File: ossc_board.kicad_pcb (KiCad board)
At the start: 2 copper layers, 91.2 x 167 mm, 343 parts, among them J1 HDMI_CONN (10029449-111RLF), J10 COLOR INPUT, J11 MONO INPUT, J12 NEXT PWR INPUT 1, J13 NEXT PWR INPUT 2, J14 -12VDC OUT, J15 5VDC STANDBY, J16 MON IN 1, J17 MON IN 2, J18 PA1, J19 BOOT0, J2 OUT (SJ1-3535NG), J20 PC0, J21 PC1, J22 PB0, J23 PB1, J24 R SPK, J25 R SPEAKER (SJ-2509N), J26 L SPEAKER, J27 L SPK, J28 I2C Ext, J29 OLED, J3 MIC (SJ1-3535NG), J30 BOOT1, J31 NeXT Keyboard, J32 NeXT Keyboard (MD-50SM / KMDG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, J4 USB Host (SS-52100-001), J5 Mic IN, J6 Audio OUT, J7 STLINK, J8 UART2, J9 PA0, P1 JTAG (30310-6002HB), Q1 2SC2712, SW1 NeXT POWER SW (1-1825027-1 / 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, SW2 BTN0, SW3 NeXT POWER SW, SW4 MCU RESET, U1 TVP7002PZP, U10 S25FL216K (IS25LP016D-JBLE), U11 TLV70033DDCR, U12 TLV70012DDCT, U13 TLV70025DDCT, U14 TLV70012DDCT, U15 TLV70018DDCT, U16 TLV70018DDCT, U17 USBLC6-2SC6, U18 STMPS2151STR‎ or TPS2051CDBV, U19 SN74LVC2G34DBV, U2 EP4CE15E22C8N, U20 PCM5122PW, U21 TLV70033DDCR (or XC6204B332MR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, U22 TLV70033DDCR (or XC6204B332MR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, U23 PLT133/T, U24 STM32F401RCT6, U25 SN74LVC1G07DBV, U26 SN74HCT125DR, U27 TLV320ADC3100, U28 BD33FC0FP, U29 TPA2005D1DGN, U3 IT6613E, U30 BD33FC0FP, U31 TPA2005D1DGN, U32 PCA9515AD, U4 SN74LVC2G17DBV, U5 BD33FC0FP, U6 TLV70033DDCR, U7 NCP703SN19T1G, U8 5V(DC/DC), U9 TLV70019DDCT, X1 ACHL-27MHZ-EK, X2 ASEDV-27.000MHZ-LR-T(ECS-2333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, X3 ECS-2520MVLC-225.792-BN-TR, Y2 25MHz (FA-238 25.0000MB-K0)

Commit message: update value
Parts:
- U26: value SN74HCT125DR -> SN74HC125DR
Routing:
- net GND: track 860.5 -> 860.1 mm, vias 373 -> 374
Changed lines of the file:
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@@
     (thickness 1.6)
     (drawings 182)
-    (tracks 4848)
+    (tracks 4852)
     (zones 0)
     (modules 343)
@@
       (effects (font (size 1 1) (thickness 0.15)) (justify mirror))
     )
-    (fp_text value SN74HCT125DR (at 0 -5.28 90) (layer B.Fab)
+    (fp_text value SN74HC125DR (at 0 -5.28 90) (layer B.Fab)
       (effects (font (size 1 1) (thickness 0.15)) (justify mirror))
     )
@@
   (via (at 104.6988 86.8934) (size 0.686) (drill 0.33) (layers F.Cu B.Cu) (net 87))
   (segment (start 91.7816 103.1748) (end 91.7816 101.6508) (width 0.4) (layer F.Cu) (net 87))
-  (segment (start 92.280672 101.151728) (end 91.7816 101.6508) (width 0.4) (layer F.Cu) (net 87))
-  (segment (start 92.280672 97.917872) (end 92.280672 101.151728) (width 0.4) (layer F.Cu) (net 87))
-  (segment (start 91.8152 97.4524) (end 92.280672 97.917872) (width 0.4) (layer F.Cu) (net 87))
-  (segment (start 90.7402 97.4524) (end 91.8152 97.4524) (width 0.4) (layer F.Cu) (net 87))
-  (segment (start 91.7816 103.1748) (end 93.599 103.1748) (width 0.4) (layer F.Cu) (net 87))
   (via (at 74.1 68.233) (size 0.686) (drill 0.35) (layers F.Cu B.Cu) (net 87))
   (via (at 120.7135 131.6482) (size 0.686) (drill 0.33) (layers F.Cu B.Cu) (net 87))
@@
   (via (at 105.1306 109.59592) (size 0.686) (drill 0.33) (layers F.Cu B.Cu) (net 87))
   (via (at 95.60052 104.96296) (size 0.686) (drill 0.33) (layers F.Cu B.Cu) (net 87))
-  (via (at 93.22816 102.13848) (size 0.686) (drill 0.33) (layers F.Cu B.Cu) (net 87))
+  (via (at 93.2688 102.6414) (size 0.686) (drill 0.33) (layers F.Cu B.Cu) (net 87))
   (via (at 94.71152 95.59544) (size 0.686) (drill 0.33) (layers F.Cu B.Cu) (net 87))
   (via (at 97.39884 96.5962) (size 0.686) (drill 0.33) (layers F.Cu B.Cu) (net 87))
@@
   (segment (start 63.1952 163.4363) (end 62.2935 162.5346) (width 0.25) (layer F.Cu) (net 87))
   (segment (start 63.7032 163.4363) (end 63.1952 163.4363) (width 0.25) (layer F.Cu) (net 87))
+  (segment (start 92.7735 102.5906) (end 93.218 102.5906) (width 0.4) (layer F.Cu) (net 87))
+  (segment (start 93.218 102.5906) (end 93.2688 102.6414) (width 0.4) (layer F.Cu) (net 87))
+  (segment (start 92.1893 103.1748) (end 92.7735 102.5906) (width 0.4) (layer F.Cu) (net 87))
+  (segment (start 91.7816 103.1748) (end 92.1893 103.1748) (width 0.4) (layer F.Cu) (net 87))
+  (via (at 92.8878 97.5106) (size 0.686) (drill 0.33) (layers F.Cu B.Cu) (net 87))
+  (segment (start 92.280672 101.151728) (end 91.7816 101.6508) (width 0.4) (layer F.Cu) (net 87))
+  (segment (start 91.2294 97.4524) (end 92.280672 98.503672) (width 0.4) (layer F.Cu) (net 87))
+  (segment (start 92.280672 98.503672) (end 92.280672 101.151728) (width 0.4) (layer F.Cu) (net 87))
+  (segment (start 90.7402 97.4524) (end 91.2294 97.4524) (width 0.4) (layer F.Cu) (net 87))
   (segment (start 51.435 83.2625) (end 50.8 83.8975) (width 0.2) (layer F.Cu) (net 88))
   (segment (start 51.435 81.0308) (end 51.435 83.2625) (width 0.2) (layer F.Cu) (net 88))
@@
     )
   )
-  (zone (net 0) (net_name "") (layer F.Cu) (hatch edge 0.508)
-    (connect_pads (clearance 0.2))
-    (min_thickness 0.254)
-    (keepout (tracks allowed) (vias allowed) (copperpour not_allowed))
-    (fill (arc_segments 32) (thermal_gap 0.508) (thermal_bridge_width 0.508))
-    (polygon
-      (pts
-        (xy 87.9348 96.1898) (xy 91.7702 96.1898) (xy 92.7608 97.1804) (xy 92.7608 104.0638) (xy 89.027 104.0638)
-        (xy 89.027 102.0064) (xy 87.9348 100.9142)
-      )
-    )
-  )
   (zone (net 0) (net_name "") (layers F&B.Cu) (hatch edge 0.508)
     (connect_pads (clearance 0.2))
@@
       )
     )
+  )
+  (zone (net 0) (net_name "") (layer F.Cu) (hatch edge 0.508)
+    (connect_pads (clearance 0.2))
+    (min_thickness 0.254)
+    (keepout (tracks allowed) (vias allowed) (copperpour not_allowed))
+    (fill (arc_segments 32) (thermal_gap 0.508) (thermal_bridge_width 0.508))
+    (polygon
+      (pts
+        (xy 87.9348 96.1898) (xy 91.5289 96.1898) (xy 92.7608 97.4217) (xy 92.7608 104.0638) (xy 89.027 104.0638)
+        (xy 89.027 102.0064) (xy 87.9348 100.9142)
+      )
+    )

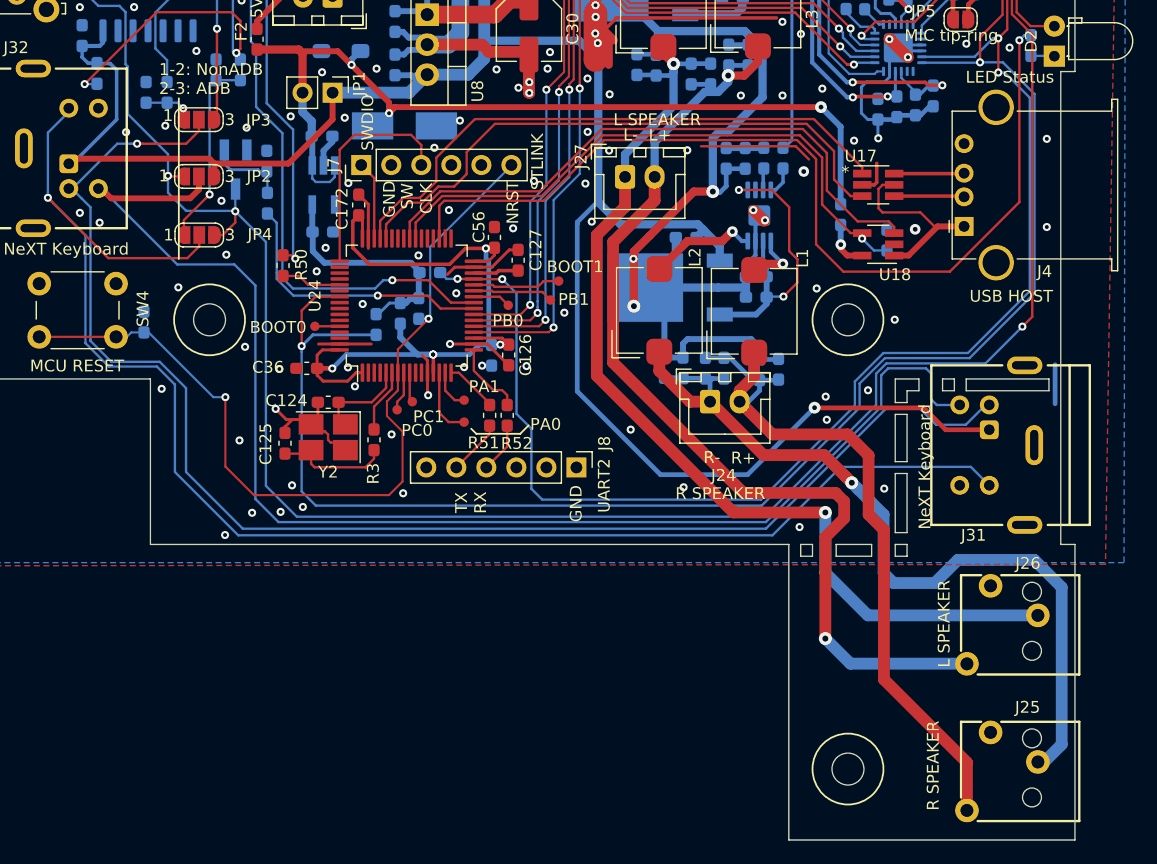
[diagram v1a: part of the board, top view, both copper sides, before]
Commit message: move keyboard DIN connector
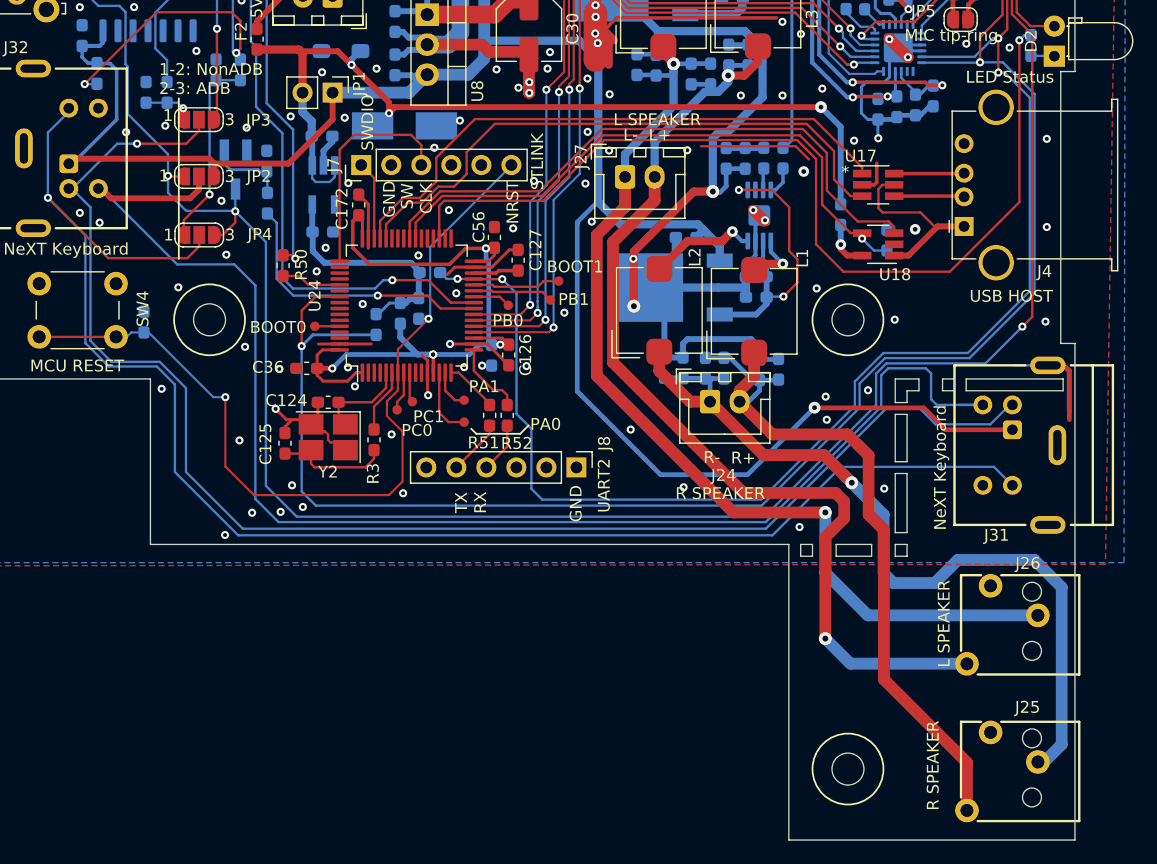
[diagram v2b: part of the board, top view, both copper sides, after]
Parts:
- moved J31 1.96 mm to (133.1, 165.6)
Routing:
- net GND: track 860.1 -> 869.8 mm, vias 374 -> 375
- net Net-(J31-Pad4): track 114.3 -> 118.5 mm
- net Net-(J31-Pad3): track 128.9 -> 130.8 mm
- net /hdmitx1/5V: track 309.6 -> 311.6 mm
- net Net-(J31-Pad2): track 119.5 -> 121.4 mm
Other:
- outline, holes or cut-outs redrawn

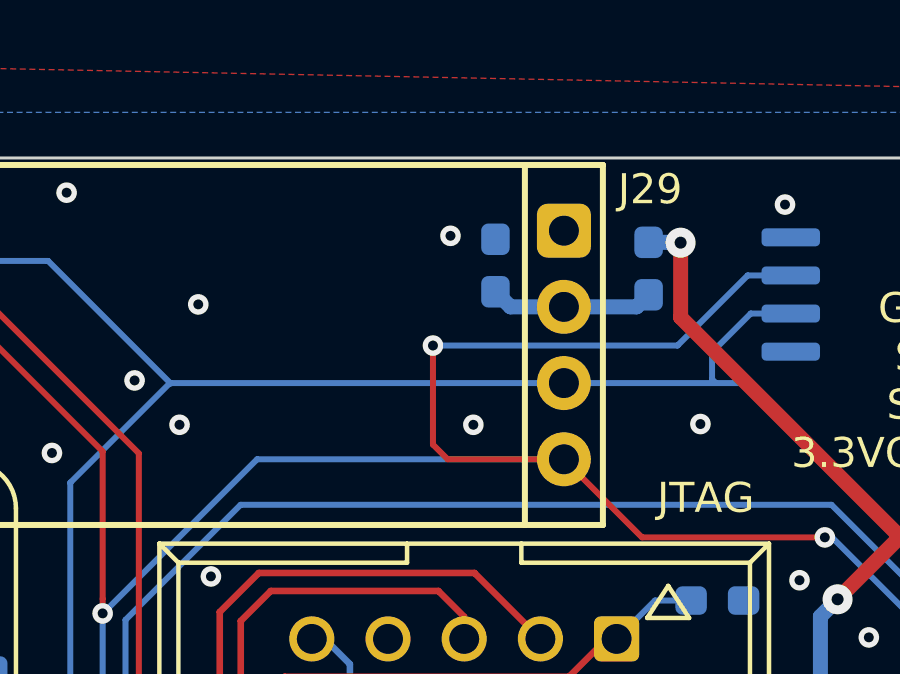
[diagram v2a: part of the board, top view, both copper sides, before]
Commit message: update silk update mount plate
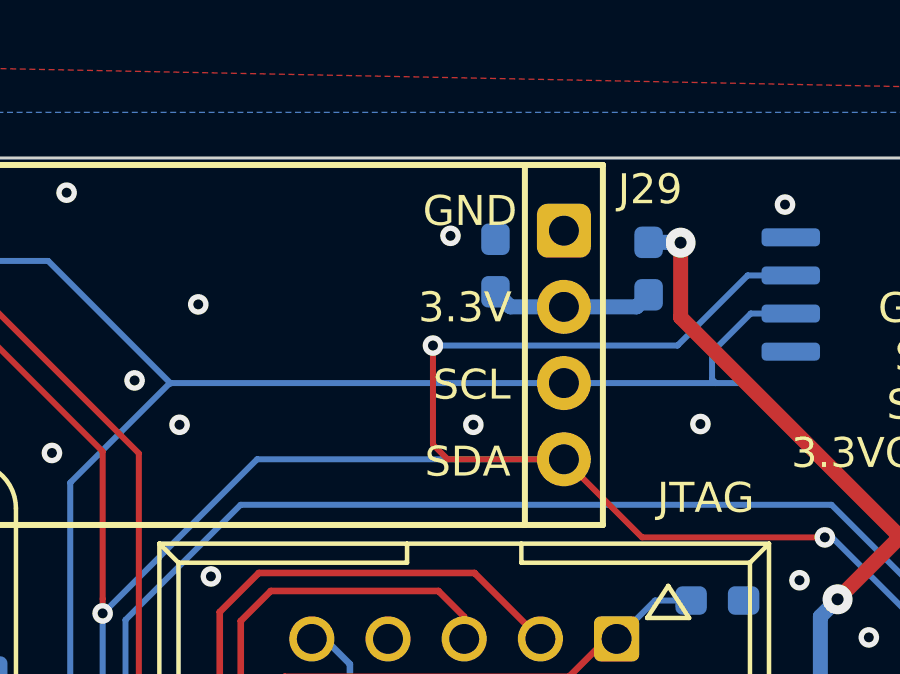
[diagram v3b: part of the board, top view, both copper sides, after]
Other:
- board text added: "3.3V"
- board text added: "SCL"
- board text added: "SDA"

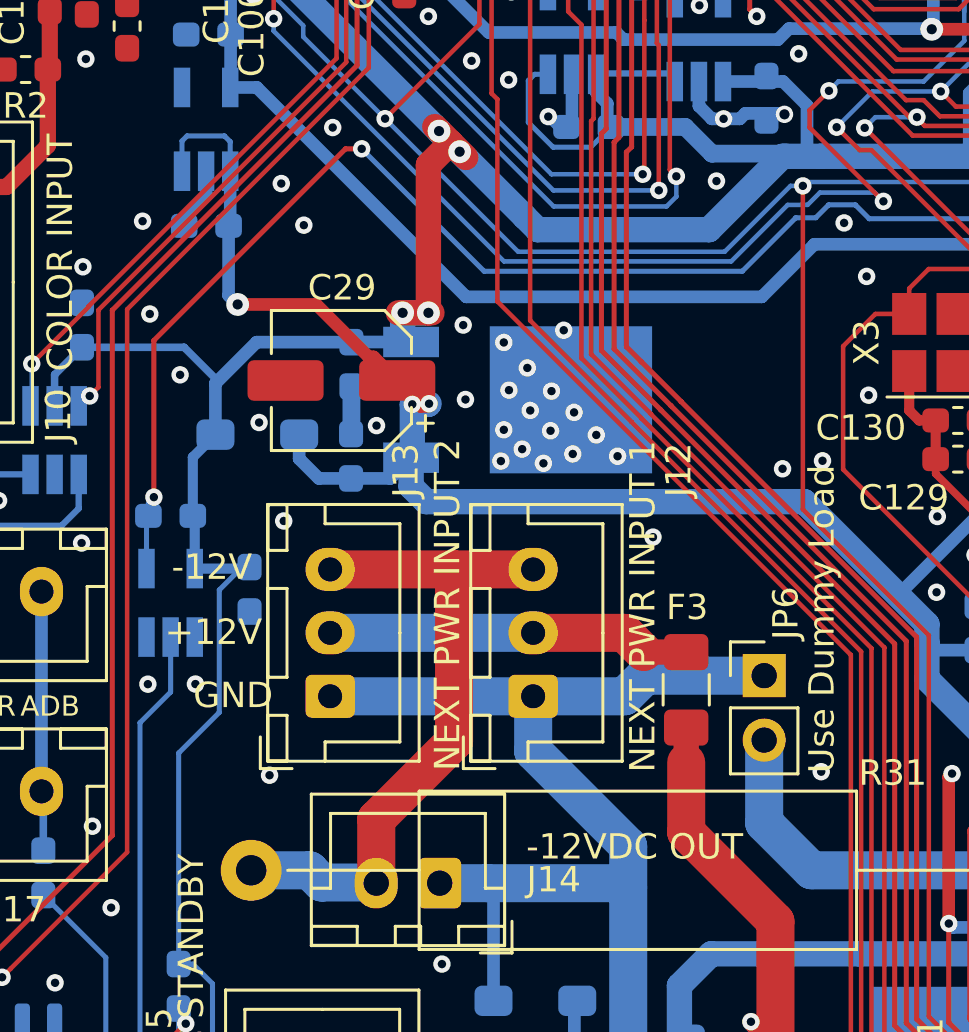
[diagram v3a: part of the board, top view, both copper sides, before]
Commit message: change 3.3V liner regulator
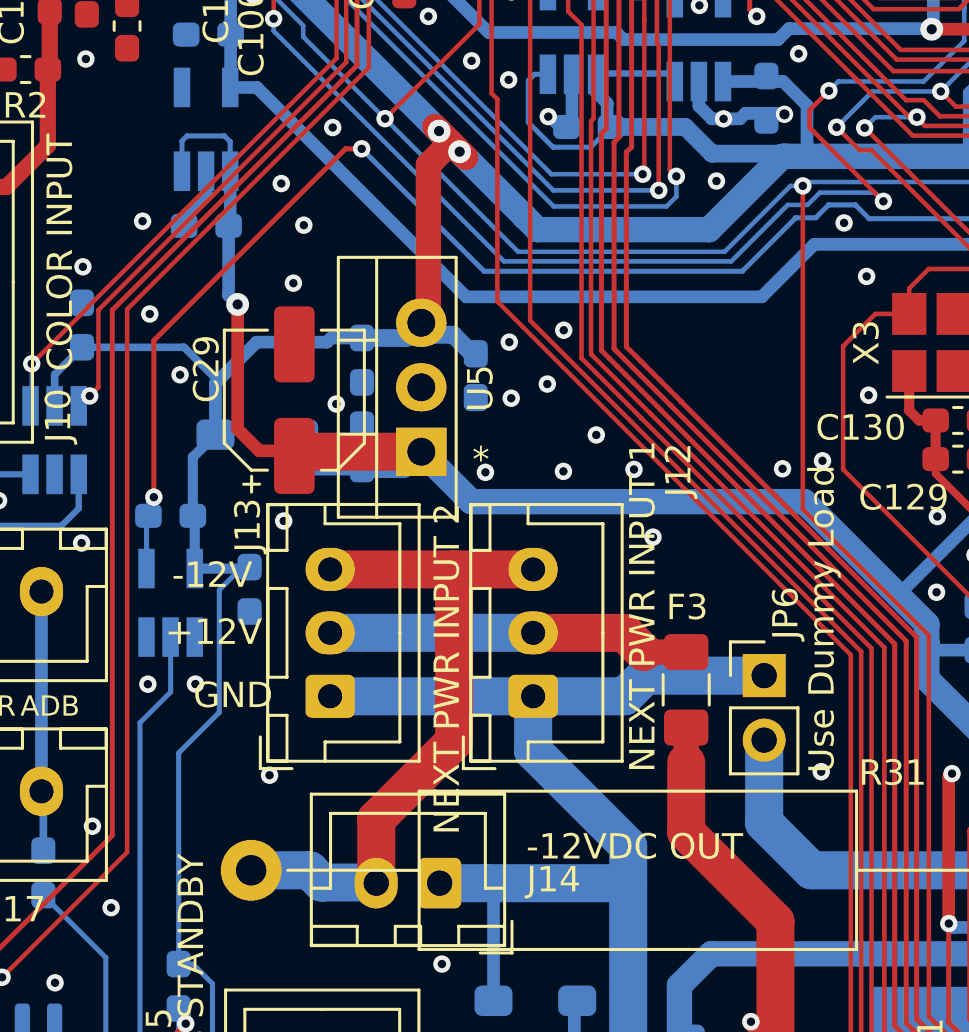
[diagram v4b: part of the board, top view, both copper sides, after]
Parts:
- added C177: 10u, Capacitor_SMD:C_0603_1608Metric_Pad1.08x0.95mm_HandSolder, B.Cu at (71.9, 99.9)
- U5: value BD33FC0FP -> MCP1826S-3302E/AB; footprint Package_TO_SOT_SMD:TO-252-2 -> Package_TO_SOT_THT:TO-220-3_Vertical; moved to F.Cu
- moved U5 4.31 mm to (69.8, 102.9), turned to 90 degrees
- moved C29 2.01 mm to (64.8, 100.9), turned to 90 degrees
- moved C31 0.57 mm to (67.4, 102.7)
- moved C93 0.45 mm to (67.4, 99.3)
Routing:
- net GND: track 869.8 -> 867.9 mm, vias 375 -> 366
- net /hdmitx1/5V: track 311.6 -> 310.7 mm, vias 5 -> 3
- net VCC: track 614.2 -> 614.5 mm, vias 34 -> 32

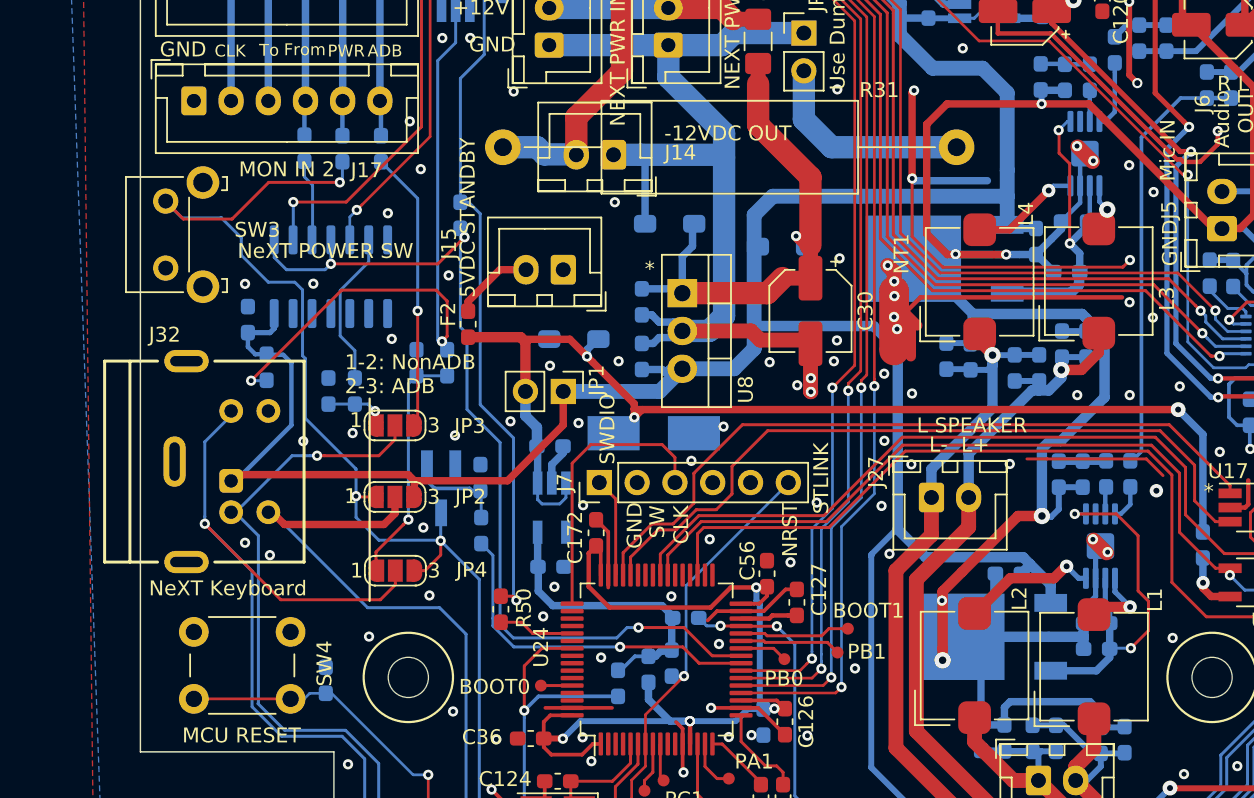
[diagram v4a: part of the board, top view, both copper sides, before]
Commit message: move front ADB connector treat shutdown pin of the amplifier
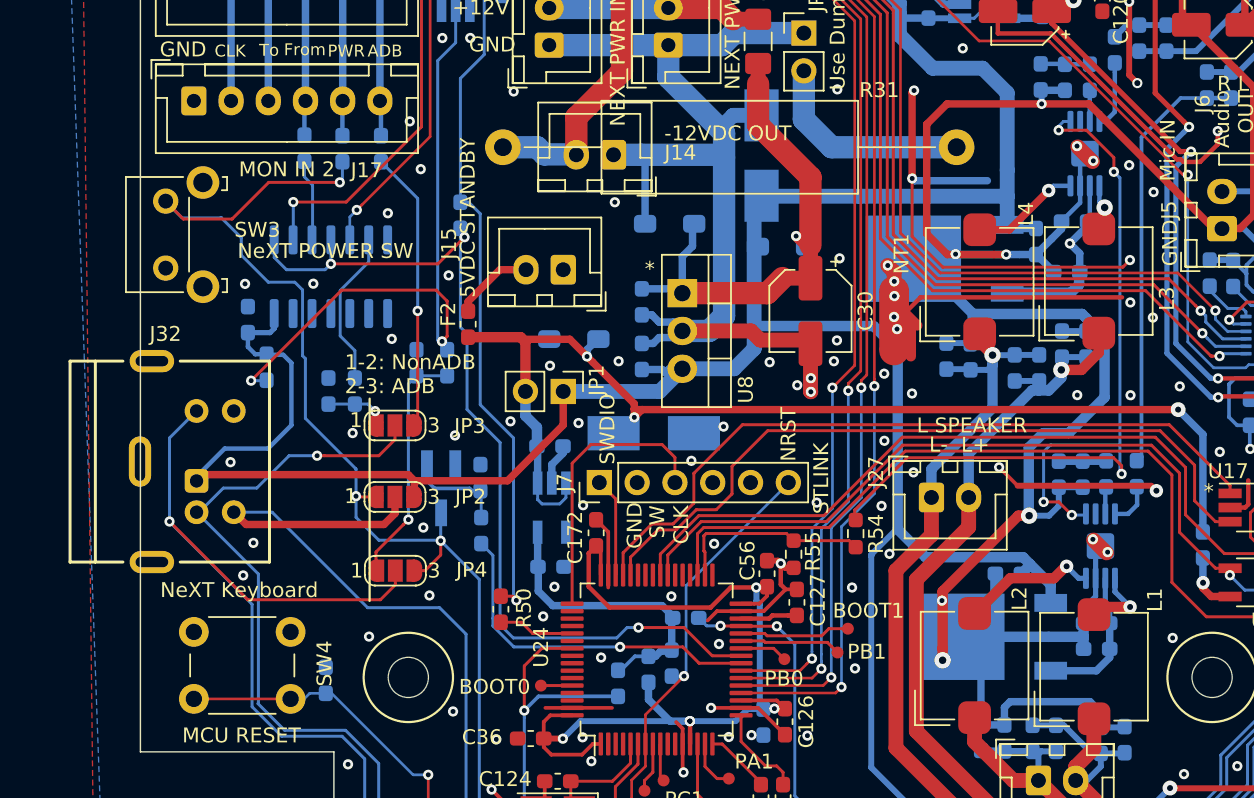
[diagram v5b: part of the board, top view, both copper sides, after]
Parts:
- added D11: (ZD 5.6V (1SMB5919BT3G)), Diode_SMD:D_SMB_Handsoldering, B.Cu at (80.4, 119.9)
- added R54: 22, Resistor_SMD:R_0603_1608Metric_Pad0.98x0.95mm_HandSolder, F.Cu at (86.8, 145.3)
- added R55: (47k), Resistor_SMD:R_0603_1608Metric_Pad0.98x0.95mm_HandSolder, F.Cu at (82.6, 146.7)
- D10: value ZD 5.6V (1SMB5919BT3G) -> (ZD 5.6V (1SMB5919BT3G))
- moved J32 2.32 mm to (34.0, 140.5)
- moved R39 0.43 mm to (105.6, 141.3)
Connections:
- U29 pad 1: Net-(C146-Pad2) -> /soundbox/AMP_SHUTDOWN
- U31 pad 1: Net-(C159-Pad2) -> /soundbox/AMP_SHUTDOWN
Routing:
- net /soundbox/AMP_SHUTDOWN: track 0.00 -> 59.8 mm, vias 0 -> 5
- net Net-(C146-Pad2): track 25.2 -> 9.85 mm, vias 2 -> 0
- net Net-(R54-Pad1): track 0.00 -> 13.3 mm
- net Net-(C159-Pad2): track 21.5 -> 12.6 mm, vias 2 -> 1
- net GND: track 867.9 -> 876.3 mm, vias 366 -> 367
- net /hdmitx1/5V: track 310.7 -> 316.1 mm
- net Net-(J31-Pad4): track 118.5 -> 123.8 mm
- net Net-(J31-Pad2): track 121.4 -> 125.1 mm
- net Net-(J31-Pad3): track 130.8 -> 134.2 mm
- net GNDA: track 325.5 -> 326.2 mm
